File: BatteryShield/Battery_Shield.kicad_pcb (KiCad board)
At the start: 2 copper layers, 95 x 123.4 mm, 60 parts, among them J100 Conn_02x02_Counter_Clockwise, J600 Conn_02x03_Counter_Clockwise, J700 MOLEX-MINIFIT-JR-5556, K100 G5LE-14 DC3, K101 G5LE-14 DC3, K200 G5LE-14 DC3, Q100 ZVN4525G, Q101 ZVN4525G, Q200 ZVN4525G, U300 LTC4151IMS-1, U301 MOCD207M, U302 MOCD207M, U400 ADC081C021, U401 LM35-D, U600 LT8608, U601 LTC3642-3.3

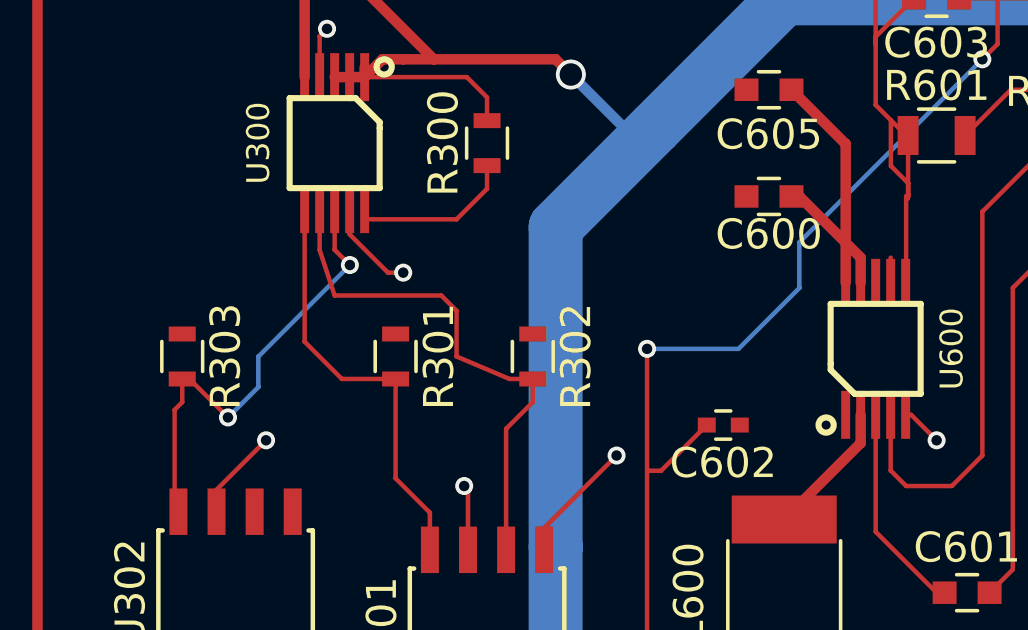
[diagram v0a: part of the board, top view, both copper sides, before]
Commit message: Added some small traces
oops I forgot them originally
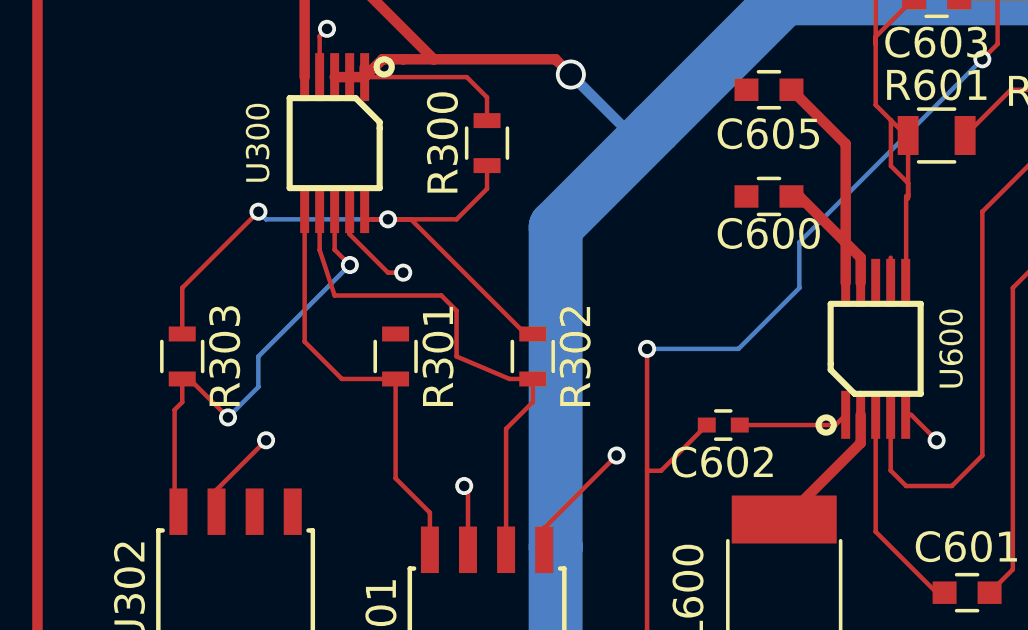
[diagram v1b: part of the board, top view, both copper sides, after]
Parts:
- D520, D521: value DZ2W03600L -> (none)
- J100: value Conn_02x02_Counter_Clockwise -> (none)
- Q200: value ZVN4525G -> (none)
- R201: value powerRes -> (none)
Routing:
- net Net-(R300-Pad1): track 5.60 -> 22.1 mm, vias 0 -> 2
- net Net-(C602-Pad1): track 0.02 -> 3.69 mm
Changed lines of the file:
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@@
   (general
     (links 143)
-    (no_connects 14)
+    (no_connects 11)
     (area 81.712999 36.500999 176.859001 160.095001)
     (thickness 1.6)
     (drawings 5)
-    (tracks 541)
+    (tracks 554)
     (zones 0)
     (modules 60)
@@
       (effects (font (size 1 1) (thickness 0.15)))
     )
-    (fp_text value DZ2W03600L (at 0 1.9 360) (layer F.Fab)
+    (fp_text value " " (at 0 1.9 360) (layer F.Fab)
       (effects (font (size 1 1) (thickness 0.15)))
     )
@@
       (effects (font (size 1 1) (thickness 0.15)))
     )
-    (fp_text value DZ2W03600L (at 0 1.9 90) (layer F.Fab)
+    (fp_text value " " (at 0 1.9 90) (layer F.Fab)
       (effects (font (size 1 1) (thickness 0.15)))
     )
@@
       (effects (font (size 1 1) (thickness 0.15)))
     )
-    (fp_text value Conn_02x02_Counter_Clockwise (at 2.1 -4) (layer F.Fab)
+    (fp_text value "" (at 3.302 -9.652) (layer F.Fab)
       (effects (font (size 1 1) (thickness 0.15)))
     )
@@
       (effects (font (size 1 1) (thickness 0.15)))
     )
-    (fp_text value ZVN4525G (at 0 2.5 270) (layer F.Fab)
+    (fp_text value " " (at 0 2.5 270) (layer F.Fab)
       (effects (font (size 1 1) (thickness 0.15)))
     )
@@
       (effects (font (size 1 1) (thickness 0.15)))
     )
-    (fp_text value powerRes (at 0 6.65 90) (layer F.Fab)
+    (fp_text value " " (at 0 6.65 90) (layer F.Fab)
       (effects (font (size 1 1) (thickness 0.15)))
     )
@@
   (segment (start 121.92 123.444) (end 123.952 125.476) (width 0.15) (layer F.Cu) (net 5))
   (segment (start 123.952 125.476) (end 124.218 125.476) (width 0.15) (layer F.Cu) (net 5))
+  (segment (start 117.39 119.888) (end 120.58 119.888) (width 0.15) (layer F.Cu) (net 6) (status 400000))
+  (segment (start 120.58 119.888) (end 120.92 119.548) (width 0.15) (layer F.Cu) (net 6) (status 800000))
   (segment (start 120.904 120.072) (end 120.92 120.056) (width 0.15) (layer F.Cu) (net 6) (status 30))
   (segment (start 122.936 112.268) (end 122.936 115.132) (width 0.15) (layer F.Cu) (net 7))
@@
   (segment (start 125.476 77.216) (end 130.556 77.216) (width 1.8) (layer B.Cu) (net 29))
   (segment (start 110.744 77.216) (end 125.476 77.216) (width 1.8) (layer B.Cu) (net 29))
+  (segment (start 98.806 116.852) (end 98.806 115.316) (width 0.15) (layer F.Cu) (net 30) (status 400000))
+  (via (at 105.664 113.03) (size 0.6) (drill 0.35) (layers F.Cu B.Cu) (net 30))
+  (segment (start 101.6 113.03) (end 105.664 113.03) (width 0.15) (layer B.Cu) (net 30))
+  (segment (start 101.346 112.776) (end 101.6 113.03) (width 0.15) (layer B.Cu) (net 30))
+  (via (at 101.346 112.776) (size 0.6) (drill 0.35) (layers F.Cu B.Cu) (net 30))
+  (segment (start 98.806 115.316) (end 101.346 112.776) (width 0.15) (layer F.Cu) (net 30))
+  (segment (start 110.49 116.852) (end 110.248 116.852) (width 0.15) (layer F.Cu) (net 30) (status C00000))
+  (segment (start 110.248 116.852) (end 106.426 113.03) (width 0.15) (layer F.Cu) (net 30) (status 400000))
+  (segment (start 106.426 113.03) (end 105.664 113.03) (width 0.15) (layer F.Cu) (net 30))
+  (segment (start 105.664 113.03) (end 105.156 113.03) (width 0.15) (layer F.Cu) (net 30))
   (segment (start 108.966 111.24) (end 108.966 112.014) (width 0.15) (layer F.Cu) (net 30))
-  (segment (start 107.95 113.03) (end 104.902 113.03) (width 0.15) (layer F.Cu) (net 30) (status 20))
+  (segment (start 107.95 113.03) (end 105.156 113.03) (width 0.15) (layer F.Cu) (net 30) (status 20))
+  (segment (start 105.156 113.03) (end 104.902 113.03) (width 0.15) (layer F.Cu) (net 30) (status 20))
   (segment (start 108.966 112.014) (end 107.95 113.03) (width 0.15) (layer F.Cu) (net 30))
   (segment (start 104.902 113.03) (end 104.886 112.69) (width 0.15) (layer F.Cu) (net 30) (status 30))

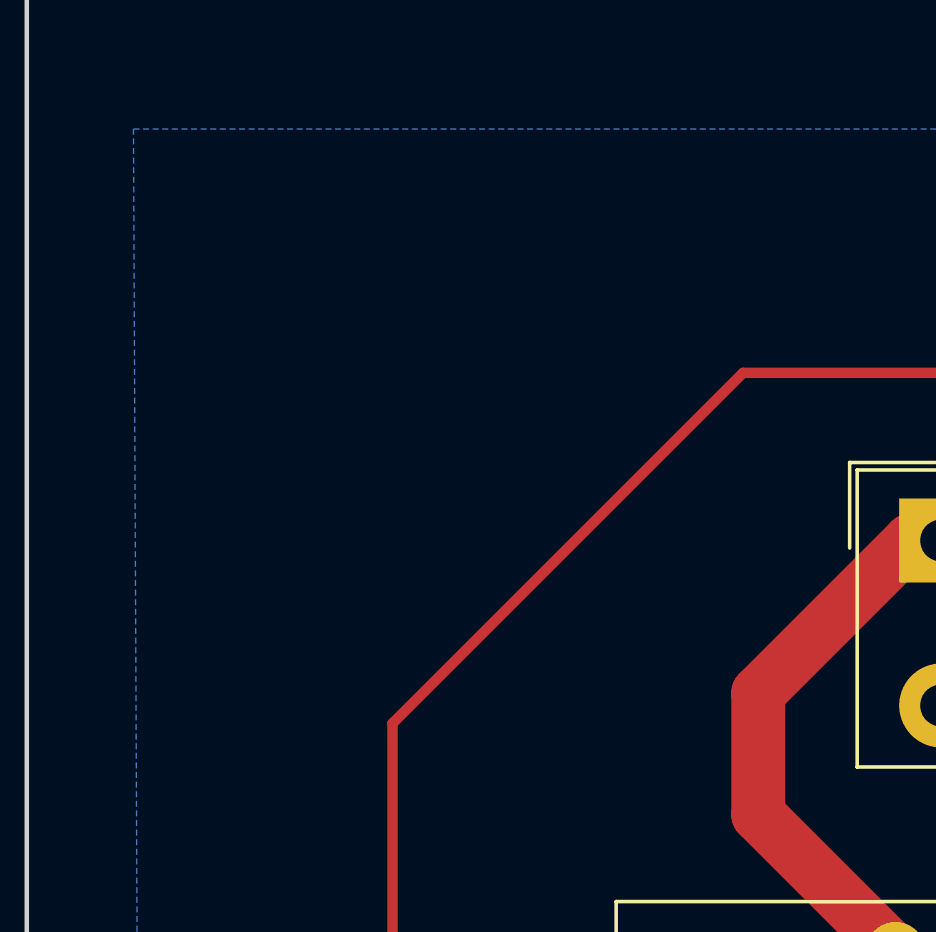
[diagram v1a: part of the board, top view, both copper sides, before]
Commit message: added logo to board
Added logo to board. KiCad needs to step up their resizing game
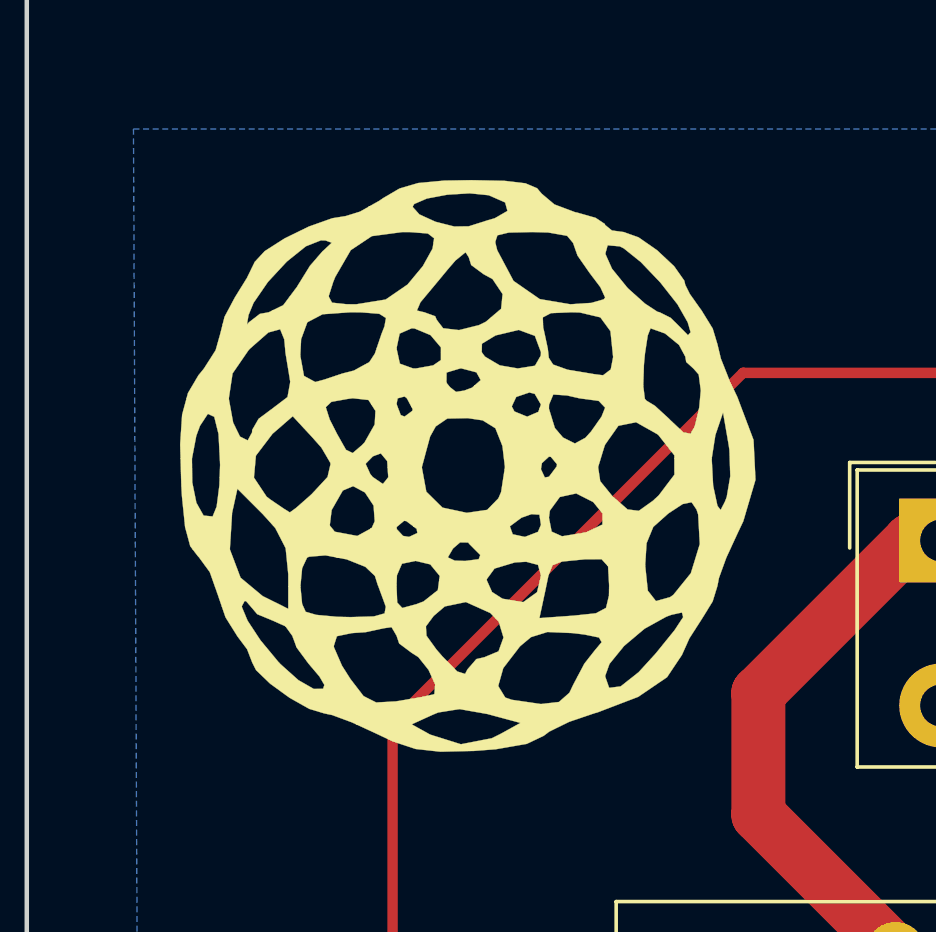
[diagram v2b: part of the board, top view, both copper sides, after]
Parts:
- added G***: LOGO, footprints:logoSmall, F.Cu at (96.5, 53.1)

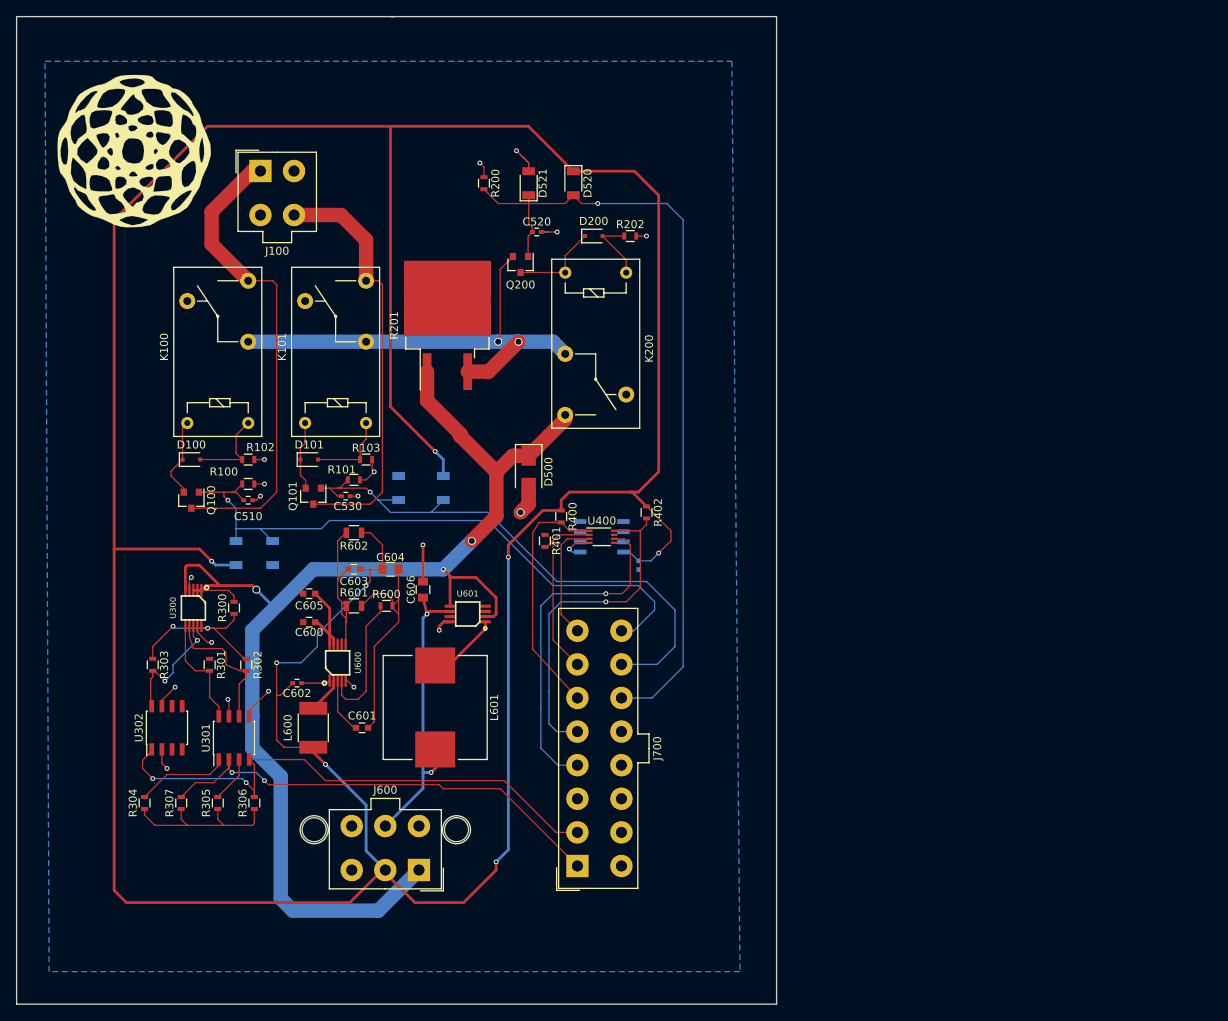
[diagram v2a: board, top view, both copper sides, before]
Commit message: fixed transistors
Fixed transistor issue with precharge circuit, added some extra optional bom modifications
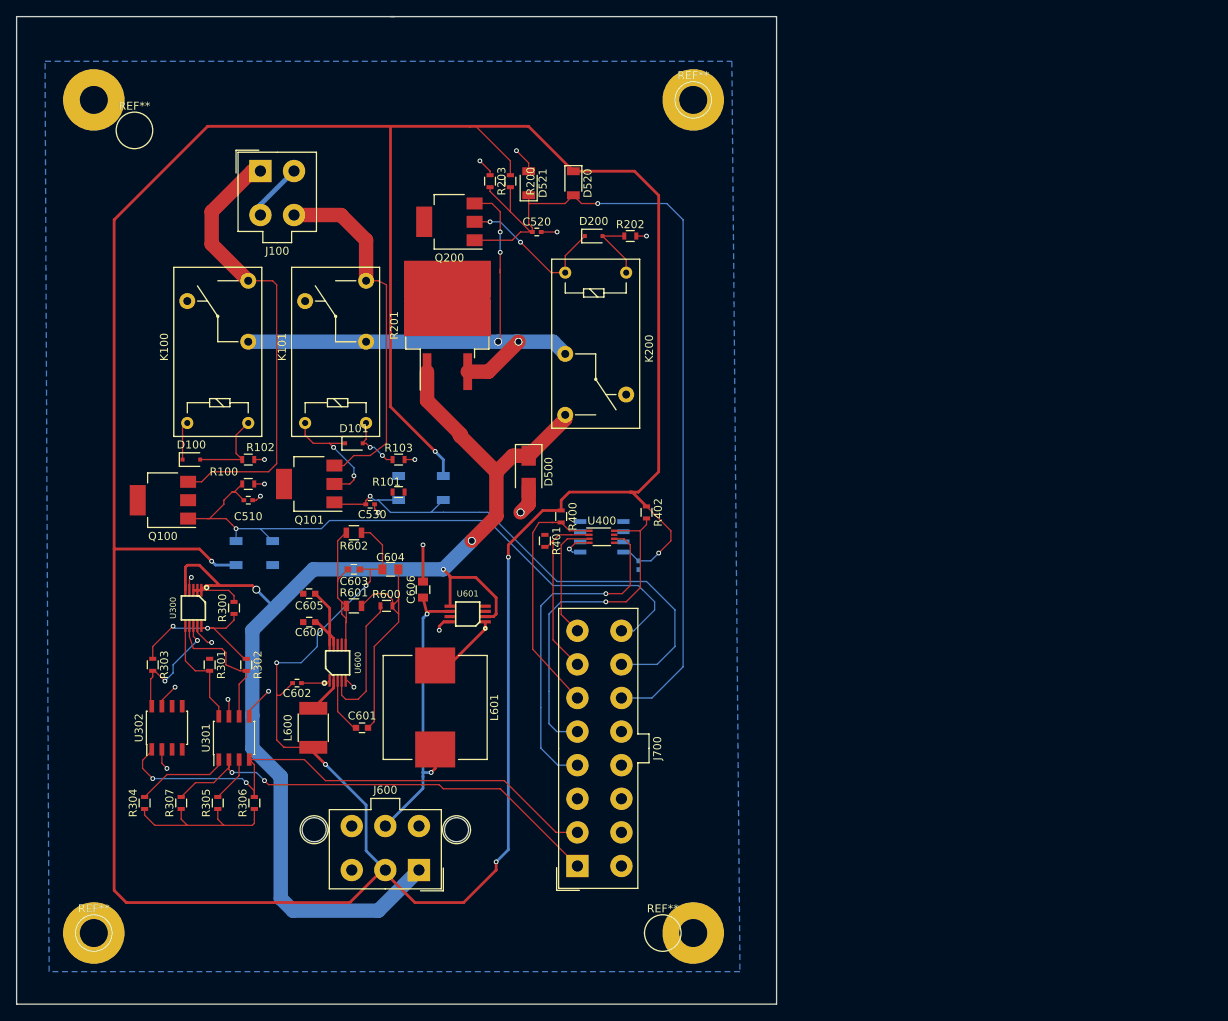
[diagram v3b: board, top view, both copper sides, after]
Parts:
- added R203: 1k, Resistors_SMD:R_0603, F.Cu at (141.0, 57.1)
- added REF**: 1pin, Connectors:1pin, F.Cu at (166.4, 47.0)
- added REF**: 1pin, Connectors:1pin, F.Cu at (162.6, 151.1)
- added REF**: 1pin, Connectors:1pin, F.Cu at (91.4, 151.1)
- added REF**: 1pin, Connectors:1pin, F.Cu at (96.5, 50.8)
- D520, D521: value (none) -> DZ2W03600L
- G***: moved to B.Cu
- J100: value (none) -> Conn_02x02_Counter_Clockwise
- Q100, Q101: value ZVN4525G -> ZVP4525G; footprint TO_SOT_Packages_SMD:SOT-23 -> TO_SOT_Packages_SMD:SOT-223
- Q200: value (none) -> ZVP4525G; footprint TO_SOT_Packages_SMD:SOT-23 -> TO_SOT_Packages_SMD:SOT-223
- R201: value (none) -> powerRes
- moved G*** 31.8 mm to (128.3, 54.6)
- moved Q200 10.4 mm to (135.9, 62.2), turned to 180 degrees
- moved D101 5.95 mm to (124.0, 89.9)
- moved R101 5.79 mm to (129.5, 96.0)
- moved R103 4.06 mm to (129.5, 91.9)
- moved Q100 3.56 mm to (100.1, 97.0), turned to 180 degrees
- moved R200 3.31 mm to (143.5, 57.1), turned to 90 degrees
- moved C530 3.21 mm to (126.0, 97.5)
- moved Q101 1.61 mm to (118.4, 95.0), turned to 180 degrees
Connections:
- Q200 pad 2: V_BATT37_PC -> Net-(D200-Pad1)
- Q200 pad 3: Net-(D200-Pad1) -> V_BATT37_PC
- R200 pad 1: BBB_GND -> PRECHARGE_N
- R200 pad 2: PRECHARGE_N -> 5V_REG
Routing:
- net PRECHARGE_N: track 100.6 -> 109.6 mm
- net V_BATT37_PC: track 59.8 -> 68.8 mm, vias 2 -> 4
- net 5V_REG: track 458.0 -> 466.7 mm
- net Net-(D200-Pad1): track 11.2 -> 19.6 mm, vias 0 -> 2
- net Net-(J100-Pad4): track 52.8 -> 45.4 mm
- net Net-(J100-Pad2): track 0.00 -> 7.24 mm
- net Net-(D101-Pad1): track 9.17 -> 15.9 mm, vias 0 -> 2
- net Net-(D100-Pad1): track 10.4 -> 5.03 mm
- net PACK_B_ON_N: track 71.1 -> 66.2 mm
- net Net-(J100-Pad1): track 59.9 -> 56.9 mm
- net (no net): track 2.96 -> 0.00 mm
- net Net-(D101-Pad2): track 10.1 -> 7.33 mm, vias 0 -> 2
- net BBB_GND: track 45.5 -> 43.5 mm
- net PACK_A_ON_N: track 79.9 -> 81.8 mm
